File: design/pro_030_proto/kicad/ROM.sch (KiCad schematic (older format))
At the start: 12 parts, among them U5 SST39SF040, U6 SST39SF040, U7 SST39SF040, U8 SST39SF040

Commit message: Add interrupt glue to schematic
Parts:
- removed R1, R2, R3, R4: 4K7, rosco_m68k:R-0207_10, symbol Device:R
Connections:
- net labels added: RW, WR
- wire segments 60 -> 35
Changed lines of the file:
@@
 $Descr A4 11693 8268
 encoding utf-8
-Sheet 4 7
+Sheet 4 8
 Title "rosco_m68k Pro (030) Prototype"
 Date "2021-07-16"
@@
 Text GLabel 10200 3050 2    50   BiDi ~ 0
 D31
-$Comp
-L Device:R R1
-U 1 1 60F8DF4C
-P 1100 3950
-F 0 "R1" H 1170 3996 50  0000 L CNN
-F 1 "4K7" H 1170 3905 50  0000 L CNN
-F 2 "rosco_m68k:R-0207_10" V 1030 3950 50  0001 C CNN
-F 3 "~" H 1100 3950 50  0001 C CNN
-	1    1100 3950
-	1    0    0    -1
-$EndComp
-$Comp
-L Device:R R2
-U 1 1 60F8F30B
-P 3700 4000
-F 0 "R2" H 3770 4046 50  0000 L CNN
-F 1 "4K7" H 3770 3955 50  0000 L CNN
-F 2 "rosco_m68k:R-0207_10" V 3630 4000 50  0001 C CNN
-F 3 "~" H 3700 4000 50  0001 C CNN
-	1    3700 4000
-	1    0    0    -1
-$EndComp
-$Comp
-L Device:R R3
-U 1 1 60F8FB9F
-P 6150 4000
-F 0 "R3" H 6220 4046 50  0000 L CNN
-F 1 "4K7" H 6220 3955 50  0000 L CNN
-F 2 "rosco_m68k:R-0207_10" V 6080 4000 50  0001 C CNN
-F 3 "~" H 6150 4000 50  0001 C CNN
-	1    6150 4000
-	1    0    0    -1
-$EndComp
-$Comp
-L Device:R R4
-U 1 1 60F90337
-P 8550 4000
-F 0 "R4" H 8620 4046 50  0000 L CNN
-F 1 "4K7" H 8620 3955 50  0000 L CNN
-F 2 "rosco_m68k:R-0207_10" V 8480 4000 50  0001 C CNN
-F 3 "~" H 8550 4000 50  0001 C CNN
-	1    8550 4000
-	1    0    0    -1
-$EndComp
-Wire Wire Line
-	9000 4350 8550 4350
-Wire Wire Line
-	8550 4350 8550 4150
-Wire Wire Line
-	6150 4150 6150 4350
-Wire Wire Line
-	6150 4350 6650 4350
-Wire Wire Line
-	3700 4150 3700 4350
-Wire Wire Line
-	3700 4350 4200 4350
-Wire Wire Line
-	1100 4100 1100 4350
-Wire Wire Line
-	1100 4350 1600 4350
 Wire Wire Line
 	2200 2250 2200 1650
@@
 	1    0    0    -1
 $EndComp
-Wire Wire Line
-	1100 3800 1100 1650
-Wire Wire Line
-	1100 1650 2200 1650
-Connection ~ 2200 1650
-Wire Wire Line
-	3700 3850 3700 1650
-Connection ~ 3700 1650
-Wire Wire Line
-	3700 1650 4800 1650
-Wire Wire Line
-	6150 3850 6150 1650
 Connection ~ 6150 1650
 Wire Wire Line
 	6150 1650 7250 1650
 Wire Wire Line
-	8550 3850 8550 1650
-Connection ~ 8550 1650
-Wire Wire Line
-	8550 1650 9600 1650
-Wire Wire Line
 	4800 1650 5800 1650
 Wire Wire Line
 	6150 1050 6150 1650
-Text GLabel 6650 4650 0    50   Input ~ 0
+Text GLabel 6650 4550 0    50   Input ~ 0
 ROMEN2
-Text GLabel 4200 4650 0    50   Input ~ 0
+Text GLabel 4200 4550 0    50   Input ~ 0
 ROMEN1
-Text GLabel 1600 4650 0    50   Input ~ 0
+Text GLabel 1600 4550 0    50   Input ~ 0
 ROMEN0
-Text GLabel 9000 4650 0    50   Input ~ 0
+Text GLabel 9000 4550 0    50   Input ~ 0
 ROMEN3
 Wire Wire Line
@@
 	6150 5250 7250 5250
 Wire Wire Line
-	6650 4550 6150 4550
-Wire Wire Line
-	6150 4550 6150 5250
-Wire Wire Line
-	9000 4550 8550 4550
-Wire Wire Line
-	8550 4550 8550 5250
-Connection ~ 8550 5250
-Wire Wire Line
-	8550 5250 9600 5250
-Wire Wire Line
-	4200 4550 3700 4550
-Wire Wire Line
-	3700 4550 3700 5250
-Connection ~ 3700 5250
-Wire Wire Line
-	3700 5250 4800 5250
-Wire Wire Line
-	1600 4550 1100 4550
-Wire Wire Line
-	1100 4550 1100 5250
-Wire Wire Line
 	1100 5250 2200 5250
 Connection ~ 2200 5250
@@
 Connection ~ 3250 1650
 Wire Wire Line
-	3250 1650 3700 1650
-Wire Wire Line
 	3250 3600 3250 5250
 Connection ~ 3250 5250
 Wire Wire Line
-	3250 5250 3700 5250
-Wire Wire Line
 	5800 3600 5800 5250
 Connection ~ 5800 5250
@@
 Connection ~ 8250 1650
 Wire Wire Line
-	8250 1650 8550 1650
-Wire Wire Line
 	8250 3600 8250 5250
 Connection ~ 8250 5250
 Wire Wire Line
-	8250 5250 8550 5250
-Wire Wire Line
 	10600 3250 10600 1650
 Wire Wire Line
@@
 	10600 5250 10600 3550
 Connection ~ 9600 5250
+Wire Wire Line
+	8250 1650 9600 1650
+Wire Wire Line
+	3250 1650 4800 1650
+Text GLabel 9000 4350 0    50   Input ~ 0
+RW
+Text GLabel 6650 4350 0    50   Input ~ 0
+RW
+Text GLabel 4200 4350 0    50   Input ~ 0
+RW
+Text GLabel 1600 4350 0    50   Input ~ 0
+RW
+Wire Wire Line
+	3250 5250 4800 5250
+Wire Wire Line
+	8250 5250 9600 5250
+Text GLabel 1600 4650 0    50   Input ~ 0
+WR
+Text GLabel 4200 4650 0    50   Input ~ 0
+WR
+Text GLabel 6650 4650 0    50   Input ~ 0
+WR
+Text GLabel 9000 4650 0    50   Input ~ 0
+WR
 $EndSCHEMATC

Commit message: Interrupts + Xosera schematic, re-annotate
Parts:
- renumbered C27 to C5, C28 to C6, C29 to C7, C30 to C8
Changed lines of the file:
@@
 $Descr A4 11693 8268
 encoding utf-8
-Sheet 4 10
+Sheet 4 13
 Title "rosco_m68k Pro (030) Prototype"
 Date "2021-07-24"
@@
 Connection ~ 7250 1650
 $Comp
-L power:VCC #PWR09
+L power:VCC #PWR010
 U 1 1 60F91B93
 P 6150 1050
-F 0 "#PWR09" H 6150 900 50  0001 C CNN
+F 0 "#PWR010" H 6150 900 50  0001 C CNN
 F 1 "VCC" H 6167 1223 50  0000 C CNN
 F 2 "" H 6150 1050 50  0001 C CNN
@@
 	4800 5250 5800 5250
 $Comp
-L power:GND #PWR010
+L power:GND #PWR011
 U 1 1 60F95B18
 P 6150 5650
-F 0 "#PWR010" H 6150 5400 50  0001 C CNN
+F 0 "#PWR011" H 6150 5400 50  0001 C CNN
 F 1 "GND" H 6155 5477 50  0000 C CNN
 F 2 "" H 6150 5650 50  0001 C CNN
@@
 Connection ~ 2200 5250
 $Comp
-L Device:C C27
+L Device:C C5
 U 1 1 60F98737
 P 3250 3450
-F 0 "C27" H 3365 3496 50  0000 L CNN
+F 0 "C5" H 3365 3496 50  0000 L CNN
 F 1 "100nF" H 3365 3405 50  0000 L CNN
 F 2 "Capacitor_THT:C_Rect_L4.0mm_W2.5mm_P2.50mm" H 3288 3300 50  0001 C CNN
@@
 $EndComp
 $Comp
-L Device:C C28
+L Device:C C6
 U 1 1 60F997DB
 P 5800 3450
-F 0 "C28" H 5915 3496 50  0000 L CNN
+F 0 "C6" H 5915 3496 50  0000 L CNN
 F 1 "100nF" H 5915 3405 50  0000 L CNN
 F 2 "Capacitor_THT:C_Rect_L4.0mm_W2.5mm_P2.50mm" H 5838 3300 50  0001 C CNN
@@
 $EndComp
 $Comp
-L Device:C C29
+L Device:C C7
 U 1 1 60F9AB06
 P 8250 3450
-F 0 "C29" H 8365 3496 50  0000 L CNN
+F 0 "C7" H 8365 3496 50  0000 L CNN
 F 1 "100nF" H 8365 3405 50  0000 L CNN
 F 2 "Capacitor_THT:C_Rect_L4.0mm_W2.5mm_P2.50mm" H 8288 3300 50  0001 C CNN
@@
 $EndComp
 $Comp
-L Device:C C30
+L Device:C C8
 U 1 1 60F9C789
 P 10600 3400
-F 0 "C30" H 10715 3446 50  0000 L CNN
+F 0 "C8" H 10715 3446 50  0000 L CNN
 F 1 "100nF" H 10715 3355 50  0000 L CNN
 F 2 "Capacitor_THT:C_Rect_L4.0mm_W2.5mm_P2.50mm" H 10638 3250 50  0001 C CNN

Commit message: Unused wire removal
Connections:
- wire segments 35 -> 34
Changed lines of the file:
@@
 Wire Wire Line
 	6150 5250 7250 5250
-Wire Wire Line
-	1100 5250 2200 5250
-Connection ~ 2200 5250
 $Comp
 L Device:C C5

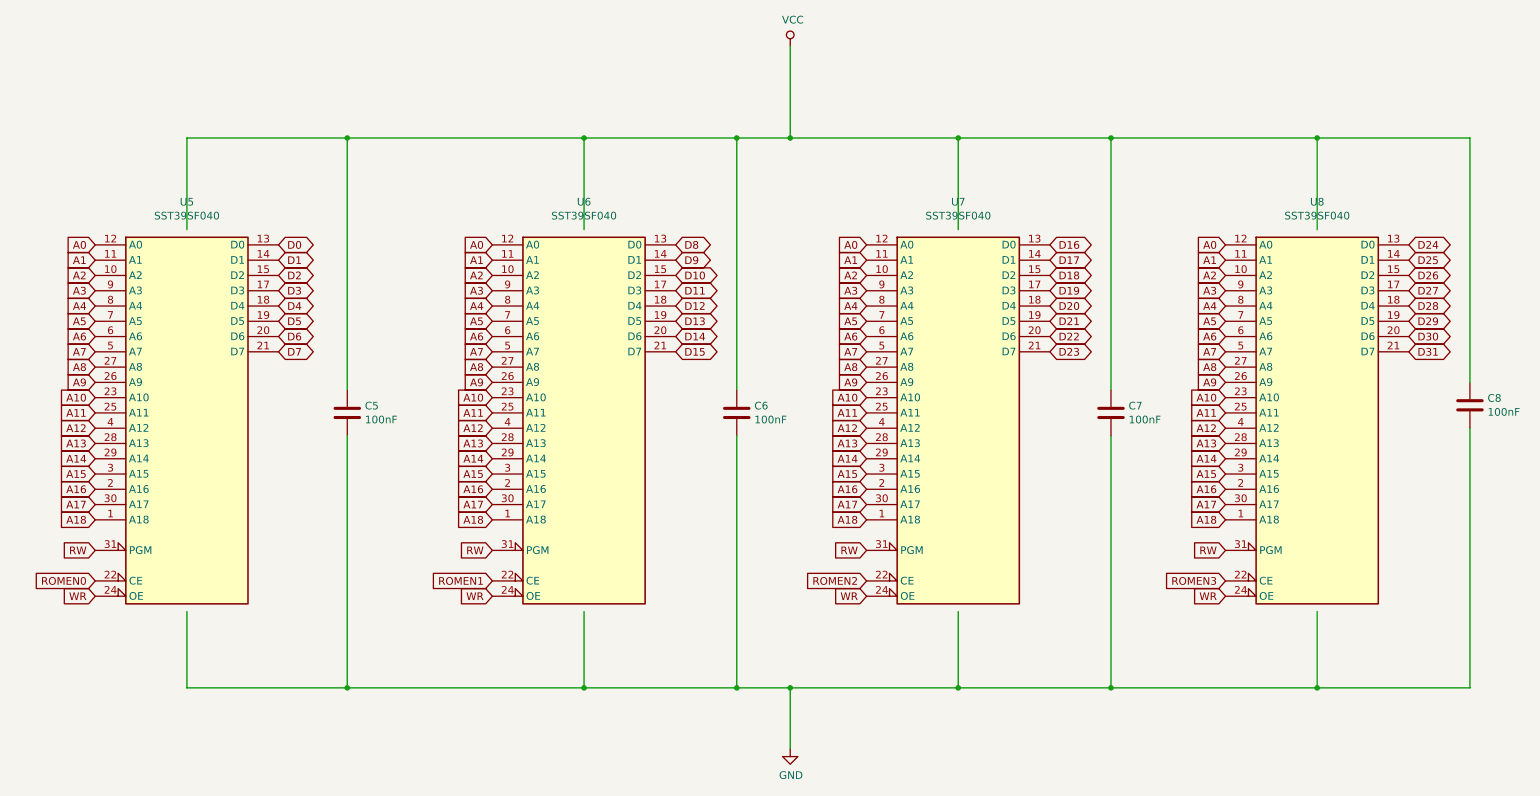
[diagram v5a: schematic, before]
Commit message: Lots more changes
* Add DIN expansion connectors (provisional pinout)
* Fix incorrect address lines for RAM & ROM (Doh!)
* Remove unused level shifters
* Fix clock enables
* Lots of other small fixes
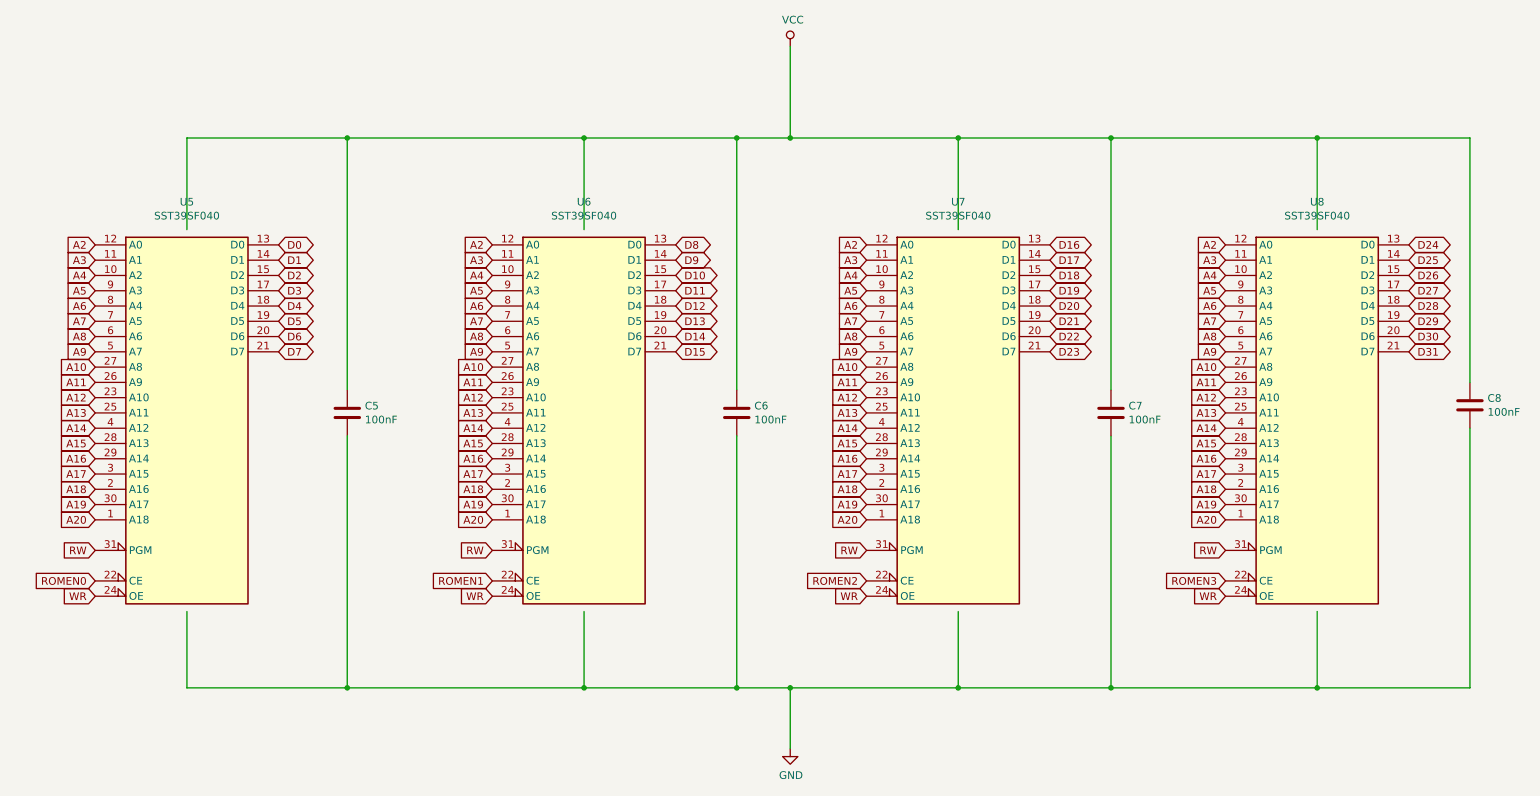
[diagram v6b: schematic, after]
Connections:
- net A0 is gone; now on net A2: U5.12 (A0), U6.12 (A0), U7.12 (A0), U8.12 (A0)
- net A1 is gone; now on net A3: U5.11 (A1), U6.11 (A1), U7.11 (A1), U8.11 (A1)
- net A10: now also U5.27 (A8), U6.27 (A8), U7.27 (A8), U8.27 (A8); no longer U5.23 (A10), U6.23 (A10), U7.23 (A10), U8.23 (A10)
- net A11: now also U5.26 (A9), U6.26 (A9), U7.26 (A9), U8.26 (A9); no longer U5.25 (A11), U6.25 (A11), U7.25 (A11), U8.25 (A11)
- net A12: now also U5.23 (A10), U6.23 (A10), U7.23 (A10), U8.23 (A10); no longer U5.4 (A12), U6.4 (A12), U7.4 (A12), U8.4 (A12)
- net A13: now also U5.25 (A11), U6.25 (A11), U7.25 (A11), U8.25 (A11); no longer U5.28 (A13), U6.28 (A13), U7.28 (A13), U8.28 (A13)
- net A14: now also U5.4 (A12), U6.4 (A12), U7.4 (A12), U8.4 (A12); no longer U5.29 (A14), U6.29 (A14), U7.29 (A14), U8.29 (A14)
- net A15: now also U5.28 (A13), U6.28 (A13), U7.28 (A13), U8.28 (A13); no longer U5.3 (A15), U6.3 (A15), U7.3 (A15), U8.3 (A15)
- net A16: now also U5.29 (A14), U6.29 (A14), U7.29 (A14), U8.29 (A14); no longer U5.2 (A16), U6.2 (A16), U7.2 (A16), U8.2 (A16)
- net A17: now also U5.3 (A15), U6.3 (A15), U7.3 (A15), U8.3 (A15); no longer U5.30 (A17), U6.30 (A17), U7.30 (A17), U8.30 (A17)
- net A18: now also U5.2 (A16), U6.2 (A16), U7.2 (A16), U8.2 (A16); no longer U5.1 (A18), U6.1 (A18), U7.1 (A18), U8.1 (A18)
- net A2: no longer U5.10 (A2), U6.10 (A2), U7.10 (A2), U8.10 (A2)
- net A3: no longer U5.9 (A3), U6.9 (A3), U7.9 (A3), U8.9 (A3)
- net A4: now also U5.10 (A2), U6.10 (A2), U7.10 (A2), U8.10 (A2); no longer U5.8 (A4), U6.8 (A4), U7.8 (A4), U8.8 (A4)
- net A5: now also U5.9 (A3), U6.9 (A3), U7.9 (A3), U8.9 (A3); no longer U5.7 (A5), U6.7 (A5), U7.7 (A5), U8.7 (A5)
- net A6: now also U5.8 (A4), U6.8 (A4), U7.8 (A4), U8.8 (A4); no longer U5.6 (A6), U6.6 (A6), U7.6 (A6), U8.6 (A6)
- net A7: now also U5.7 (A5), U6.7 (A5), U7.7 (A5), U8.7 (A5); no longer U5.5 (A7), U6.5 (A7), U7.5 (A7), U8.5 (A7)
- net A8: now also U5.6 (A6), U6.6 (A6), U7.6 (A6), U8.6 (A6); no longer U5.27 (A8), U6.27 (A8), U7.27 (A8), U8.27 (A8)
- net A9: now also U5.5 (A7), U6.5 (A7), U7.5 (A7), U8.5 (A7); no longer U5.26 (A9), U6.26 (A9), U7.26 (A9), U8.26 (A9)
- new net A19: U5.30 (A17), U6.30 (A17), U7.30 (A17), U8.30 (A17)
- new net A20: U5.1 (A18), U6.1 (A18), U7.1 (A18), U8.1 (A18)
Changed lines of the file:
@@
 $Descr A4 11693 8268
 encoding utf-8
-Sheet 4 15
+Sheet 4 14
 Title "rosco_m68k Pro (030) Prototype"
 Date "2021-10-01"
@@
 $EndComp
 Text GLabel 1600 2350 0    50   Input ~ 0
-A0
+A2
 Text GLabel 1600 2450 0    50   Input ~ 0
-A1
+A3
 Text GLabel 1600 2550 0    50   Input ~ 0
-A2
+A4
 Text GLabel 1600 2650 0    50   Input ~ 0
-A3
+A5
 Text GLabel 1600 2750 0    50   Input ~ 0
-A4
+A6
 Text GLabel 1600 2850 0    50   Input ~ 0
-A5
+A7
 Text GLabel 1600 2950 0    50   Input ~ 0
-A6
+A8
 Text GLabel 1600 3050 0    50   Input ~ 0
-A7
+A9
 Text GLabel 1600 3150 0    50   Input ~ 0
-A8
+A10
 Text GLabel 1600 3250 0    50   Input ~ 0
-A9
+A11
 Text GLabel 1600 3350 0    50   Input ~ 0
-A10
+A12
 Text GLabel 1600 3450 0    50   Input ~ 0
-A11
+A13
 Text GLabel 1600 3550 0    50   Input ~ 0
-A12
+A14
 Text GLabel 1600 3650 0    50   Input ~ 0
-A13
+A15
 Text GLabel 1600 3750 0    50   Input ~ 0
-A14
+A16
 Text GLabel 1600 3850 0    50   Input ~ 0
-A15
+A17
 Text GLabel 1600 3950 0    50   Input ~ 0
-A16
-Text GLabel 1600 4050 0    50   Input ~ 0
-A17
-Text GLabel 1600 4150 0    50   Input ~ 0
 A18
 Text GLabel 4200 2350 0    50   Input ~ 0
-A0
+A2
 Text GLabel 4200 2450 0    50   Input ~ 0
-A1
+A3
 Text GLabel 4200 2550 0    50   Input ~ 0
-A2
+A4
 Text GLabel 4200 2650 0    50   Input ~ 0
-A3
+A5
 Text GLabel 4200 2750 0    50   Input ~ 0
-A4
+A6
 Text GLabel 4200 2850 0    50   Input ~ 0
-A5
+A7
 Text GLabel 4200 2950 0    50   Input ~ 0
-A6
+A8
 Text GLabel 4200 3050 0    50   Input ~ 0
-A7
+A9
 Text GLabel 4200 3150 0    50   Input ~ 0
-A8
+A10
 Text GLabel 4200 3250 0    50   Input ~ 0
-A9
+A11
 Text GLabel 4200 3350 0    50   Input ~ 0
-A10
+A12
 Text GLabel 4200 3450 0    50   Input ~ 0
-A11
+A13
 Text GLabel 4200 3550 0    50   Input ~ 0
-A12
+A14
 Text GLabel 4200 3650 0    50   Input ~ 0
-A13
+A15
 Text GLabel 4200 3750 0    50   Input ~ 0
-A14
+A16
 Text GLabel 4200 3850 0    50   Input ~ 0
-A15
+A17
 Text GLabel 4200 3950 0    50   Input ~ 0
-A16
-Text GLabel 4200 4050 0    50   Input ~ 0
-A17
-Text GLabel 4200 4150 0    50   Input ~ 0
 A18
 Text GLabel 6650 2350 0    50   Input ~ 0
-A0
+A2
 Text GLabel 6650 2450 0    50   Input ~ 0
-A1
+A3
 Text GLabel 6650 2550 0    50   Input ~ 0
-A2
+A4
 Text GLabel 6650 2650 0    50   Input ~ 0
-A3
+A5
 Text GLabel 6650 2750 0    50   Input ~ 0
-A4
+A6
 Text GLabel 6650 2850 0    50   Input ~ 0
-A5
+A7
 Text GLabel 6650 2950 0    50   Input ~ 0
-A6
+A8
 Text GLabel 6650 3050 0    50   Input ~ 0
-A7
+A9
 Text GLabel 6650 3150 0    50   Input ~ 0
-A8
+A10
 Text GLabel 6650 3250 0    50   Input ~ 0
-A9
+A11
 Text GLabel 6650 3350 0    50   Input ~ 0
-A10
+A12
 Text GLabel 6650 3450 0    50   Input ~ 0
-A11
+A13
 Text GLabel 6650 3550 0    50   Input ~ 0
-A12
+A14
 Text GLabel 6650 3650 0    50   Input ~ 0
-A13
+A15
 Text GLabel 6650 3750 0    50   Input ~ 0
-A14
+A16
 Text GLabel 6650 3850 0    50   Input ~ 0
-A15
+A17
 Text GLabel 6650 3950 0    50   Input ~ 0
-A16
-Text GLabel 6650 4050 0    50   Input ~ 0
-A17
-Text GLabel 6650 4150 0    50   Input ~ 0
 A18
 Text GLabel 9000 2350 0    50   Input ~ 0
-A0
+A2
 Text GLabel 9000 2450 0    50   Input ~ 0
-A1
+A3
 Text GLabel 9000 2550 0    50   Input ~ 0
-A2
+A4
 Text GLabel 9000 2650 0    50   Input ~ 0
-A3
+A5
 Text GLabel 9000 2750 0    50   Input ~ 0
-A4
+A6
 Text GLabel 9000 2850 0    50   Input ~ 0
-A5
+A7
 Text GLabel 9000 2950 0    50   Input ~ 0
-A6
+A8
 Text GLabel 9000 3050 0    50   Input ~ 0
-A7
+A9
 Text GLabel 9000 3150 0    50   Input ~ 0
-A8
+A10
 Text GLabel 9000 3250 0    50   Input ~ 0
-A9
+A11
 Text GLabel 9000 3350 0    50   Input ~ 0
-A10
+A12
 Text GLabel 9000 3450 0    50   Input ~ 0
-A11
+A13
 Text GLabel 9000 3550 0    50   Input ~ 0
-A12
+A14
 Text GLabel 9000 3650 0    50   Input ~ 0
-A13
+A15
 Text GLabel 9000 3750 0    50   Input ~ 0
-A14
+A16
 Text GLabel 9000 3850 0    50   Input ~ 0
-A15
+A17
 Text GLabel 9000 3950 0    50   Input ~ 0
-A16
-Text GLabel 9000 4050 0    50   Input ~ 0
-A17
-Text GLabel 9000 4150 0    50   Input ~ 0
 A18
 Text GLabel 2800 2350 2    50   BiDi ~ 0
@@
 Text GLabel 9000 4650 0    50   Input ~ 0
 WR
+Text GLabel 1600 4050 0    50   Input ~ 0
+A19
+Text GLabel 1600 4150 0    50   Input ~ 0
+A20
+Text GLabel 4200 4050 0    50   Input ~ 0
+A19
+Text GLabel 4200 4150 0    50   Input ~ 0
+A20
+Text GLabel 6650 4050 0    50   Input ~ 0
+A19
+Text GLabel 6650 4150 0    50   Input ~ 0
+A20
+Text GLabel 9000 4050 0    50   Input ~ 0
+A19
+Text GLabel 9000 4150 0    50   Input ~ 0
+A20
 $EndSCHEMATC
